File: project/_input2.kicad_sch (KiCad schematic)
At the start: 39 parts, among them J9 input_1x5, Q10 MMBTA44, Q11 MMBTA44, Q12 MMBTA44, Q13 MMBTA44, Q14 MMBTA44, Q15 MMBTA44, Q16 MMBTA44, Q9 MMBTA44, U10 LTV-244-GB-G

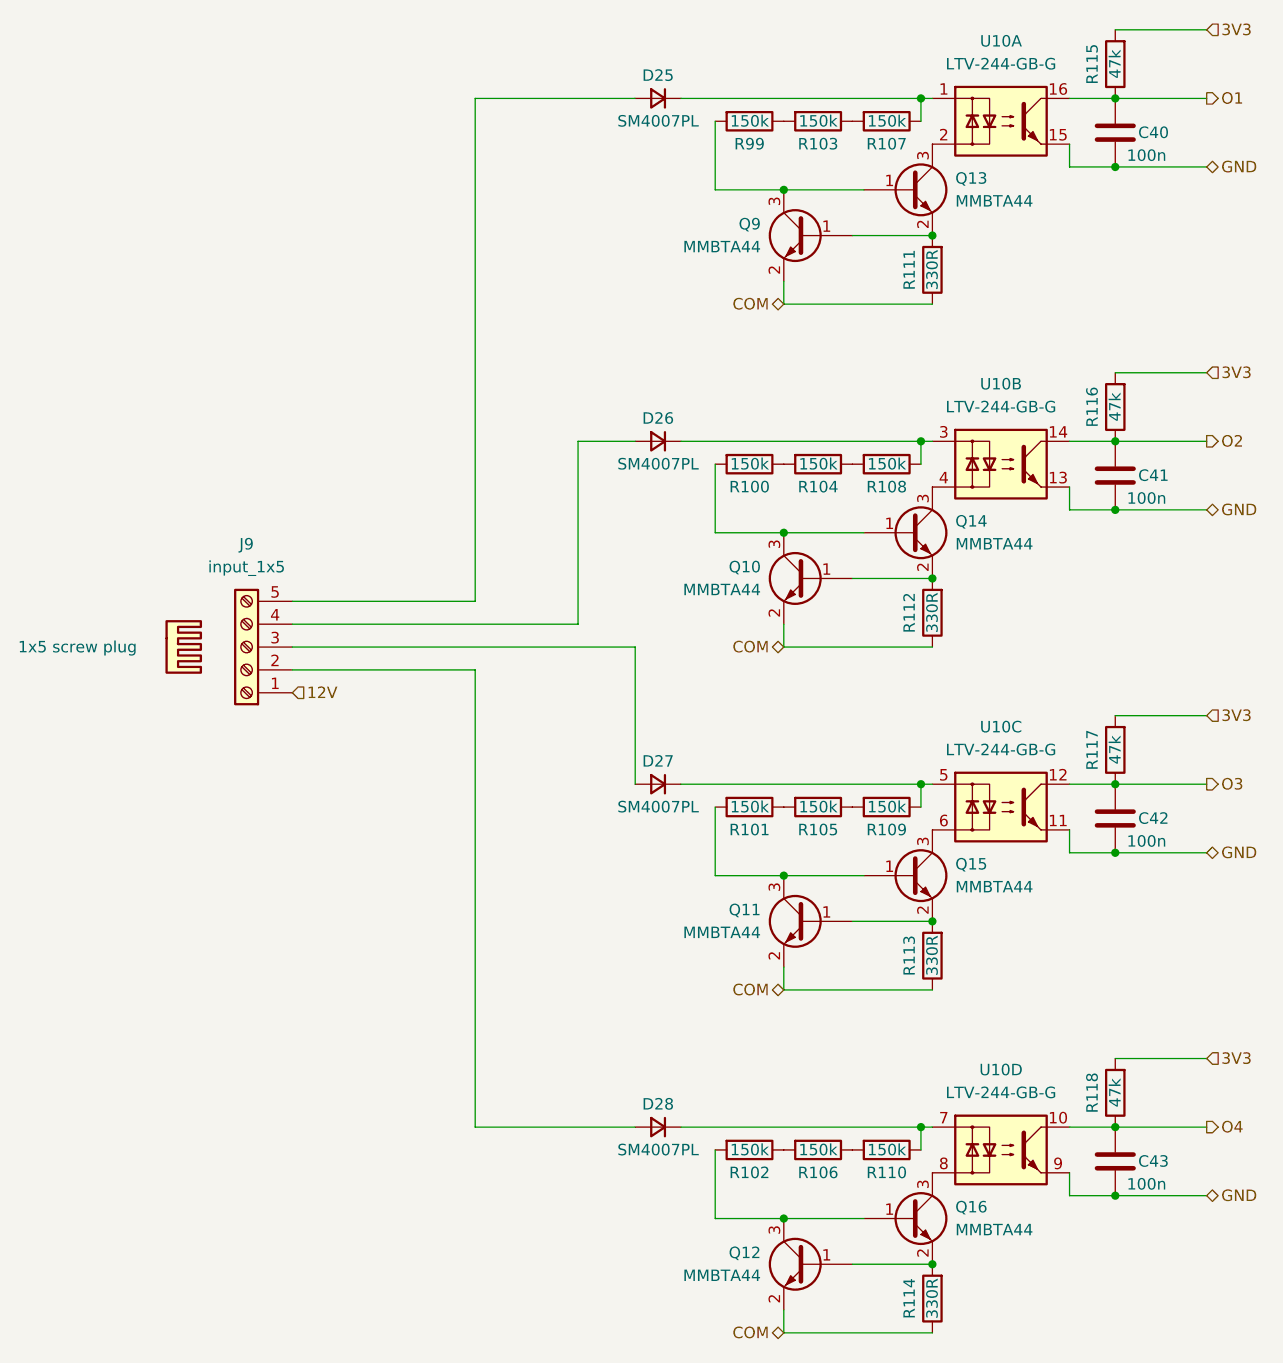
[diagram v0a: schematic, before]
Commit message: refactoring everything to use selected input type
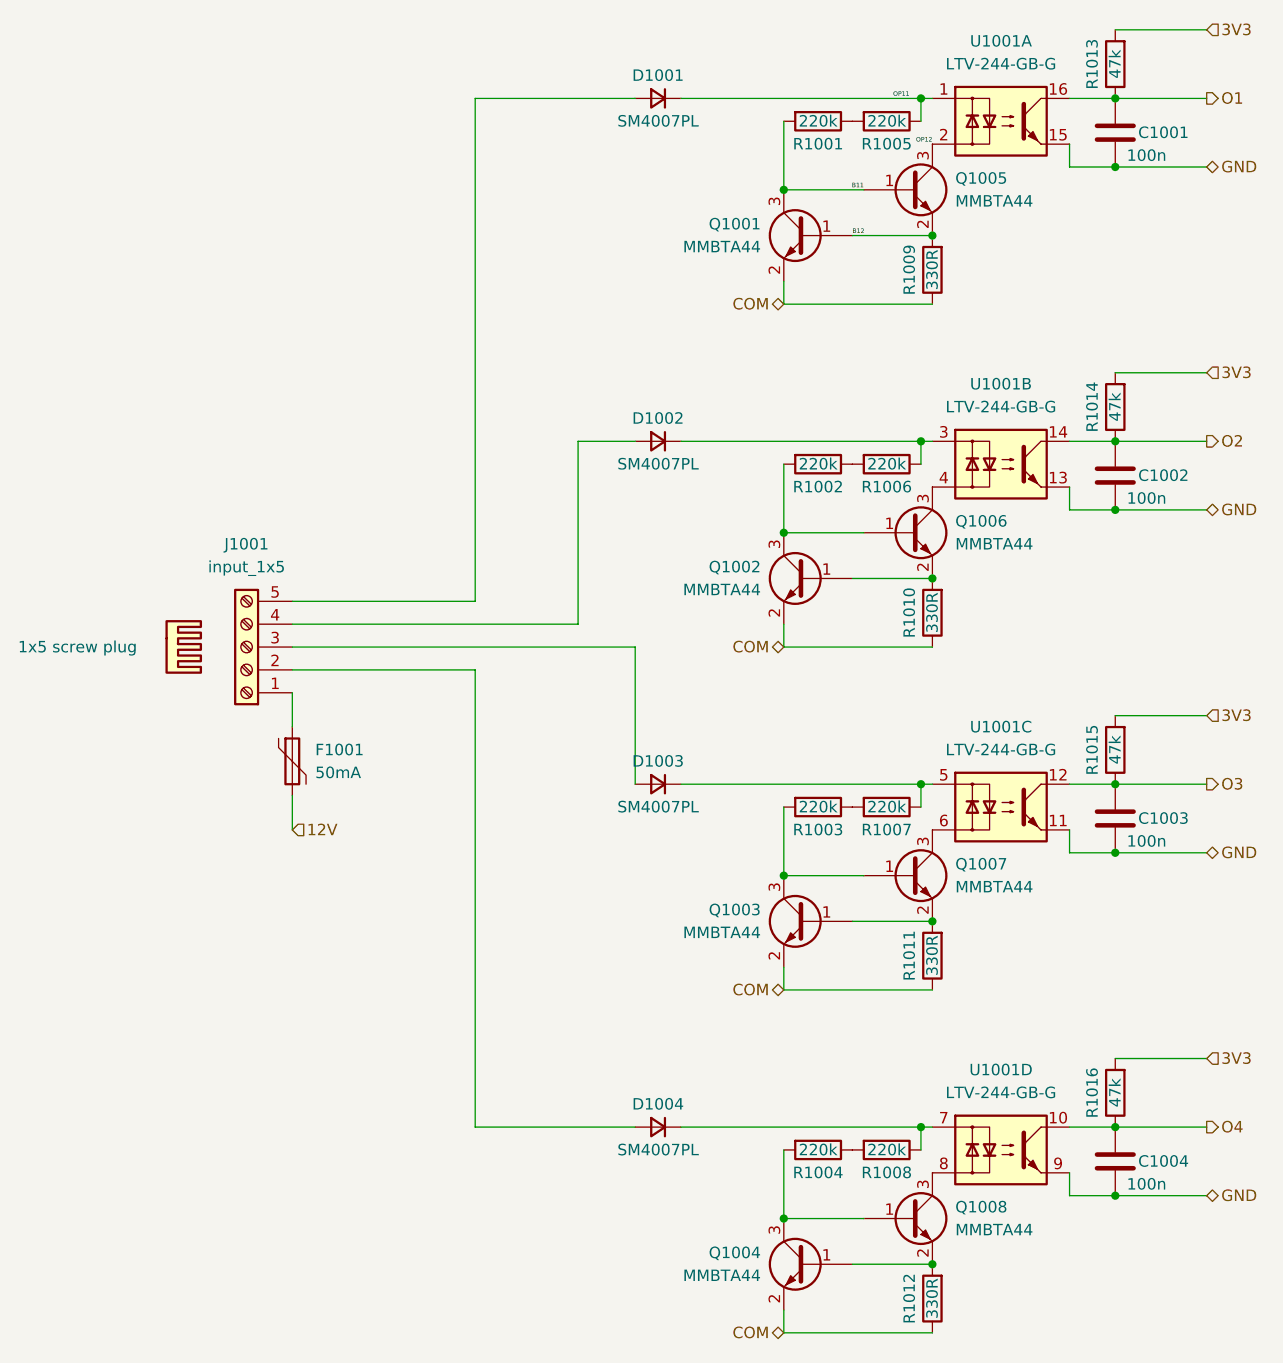
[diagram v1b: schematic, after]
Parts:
- removed C41, C42, C43: 100n, Capacitor_SMD:C_0805_2012Metric_Pad1.18x1.45mm_HandSolder, symbol Device:C
- removed D26, D27, D28: SM4007PL, Diode_SMD:D_SOD-123F, symbol Device:D_Small
- removed Q10, Q11, Q12, Q14, Q15, Q16: MMBTA44, Package_TO_SOT_SMD:SOT-23W, symbol Device:Q_NPN_BEC
- removed R100, R101, R102, R104, R105, R106, R108, R109, R110, R99: 150k, Resistor_SMD:R_0805_2012Metric_Pad1.20x1.40mm_HandSolder, symbol Device:R
- removed R112, R113, R114: 330R, Resistor_SMD:R_0805_2012Metric_Pad1.20x1.40mm_HandSolder, symbol Device:R
- removed R116, R117, R118: 47k, Resistor_SMD:R_0805_2012Metric_Pad1.20x1.40mm_HandSolder, symbol Device:R
- added C1002, C1003, C1004: 100n, Capacitor_SMD:C_0402_1005Metric_Pad0.74x0.62mm_HandSolder, symbol Device:C
- added D1002, D1003, D1004: SM4007PL, Diode_SMD:D_SOD-123F, symbol Device:D_Small
- added F1001: 50mA, Fuse:Fuse_1206_3216Metric_Pad1.42x1.75mm_HandSolder, symbol Device:Polyfuse
- added Q1002, Q1003, Q1004, Q1006, Q1007, Q1008: MMBTA44, Package_TO_SOT_SMD:SOT-23W, symbol Device:Q_NPN_BEC
- added R1002, R1003, R1004, R1006, R1007, R1008: 220k, Resistor_SMD:R_0805_2012Metric_Pad1.20x1.40mm_HandSolder, symbol Device:R
- added R1010, R1011, R1012: 330R, Resistor_SMD:R_0402_1005Metric_Pad0.72x0.64mm_HandSolder, symbol Device:R
- added R1014, R1015, R1016: 47k, Resistor_SMD:R_0402_1005Metric_Pad0.72x0.64mm_HandSolder, symbol Device:R
- C1001: renamed from C40; footprint Capacitor_SMD:C_0805_2012Metric_Pad1.18x1.45mm_HandSolder -> Capacitor_SMD:C_0402_1005Metric_Pad0.74x0.62mm_HandSolder; lcsc# C28233 -> C307331
- R1001: renamed from R103; value 150k -> 220k; lcsc# (none) -> C17556
- R1005: renamed from R107; value 150k -> 220k; lcsc# (none) -> C17556
- R1009: renamed from R111; footprint Resistor_SMD:R_0805_2012Metric_Pad1.20x1.40mm_HandSolder -> Resistor_SMD:R_0402_1005Metric_Pad0.72x0.64mm_HandSolder; lcsc# (none) -> C25104
- R1013: renamed from R115; footprint Resistor_SMD:R_0805_2012Metric_Pad1.20x1.40mm_HandSolder -> Resistor_SMD:R_0402_1005Metric_Pad0.72x0.64mm_HandSolder; lcsc# (none) -> C25792
- renumbered BOM9 to BOM1001, D25 to D1001, J9 to J1001, Q9 to Q1001, Q13 to Q1005, U10 to U1001
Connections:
- net 12V: now also F1001.2; no longer J1001.1 (Pin_1)
- net 3V3: now also R1014.2, R1015.2, R1016.2
- net COM: now also Q1002.2 (E), Q1003.2 (E), Q1004.2 (E), R1010.1, R1011.1, R1012.1
- net GND: now also C1002.2, C1003.2, C1004.2
- net O2: now also C1002.1, R1014.1
- net O3: now also C1003.1, R1015.1
- net O4: now also C1004.1, R1016.1
- net at U1001.3: now also D1002.1 (K), R1006.1
- net at U1001.5: now also D1003.1 (K), R1007.1
- net at U1001.6: now also Q1007.3 (C)
- net B11: now reaches R1001.2
- net B11: now also Q1001.3 (C), Q1005.1 (B)
- net OP11: now reaches D1001.1 (K), R1005.1, U1001.1
- net at J1001.4 (Pin_4): now also D1002.2 (A)
- net OP12: now reaches Q1005.3 (C), U1001.2
- net at U1001.4: now also Q1006.3 (C)
- net at J1001.3 (Pin_3): now also D1003.2 (A)
- net at J1001.2 (Pin_2): now also D1004.2 (A)
- net B12: now reaches Q1001.1 (B), Q1005.2 (E), R1009.2
- net at U1001.8: now also Q1008.3 (C)
- net at U1001.7: now also D1004.1 (K), R1008.1
- new net: Q1003.3 (C), Q1007.1 (B), R1003.2
- new net: Q1003.1 (B), Q1007.2 (E), R1011.2
- new net: Q1004.1 (B), Q1008.2 (E), R1012.2
- new net: Q1004.3 (C), Q1008.1 (B), R1004.2
- new net: Q1002.3 (C), Q1006.1 (B), R1002.2
- new net: Q1002.1 (B), Q1006.2 (E), R1010.2
- new net: R1003.1, R1007.2
- new net: F1001.1, J1001.1 (Pin_1)
- new net: R1004.1, R1008.2
- new net: R1002.1, R1006.2

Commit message: replacing thermometer
* Switching to TMP102 as TMP101 is no longer available
* bumping up version
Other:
- company: (none) -> makerspace.lt
- title: (none) -> WormControl-Input32-InputBoard
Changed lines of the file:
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@@
 (kicad_sch (version 20211123) (generator eeschema)
   (paper "A4")
+  (title_block
+    (title "WormControl-Input32-InputBoard")
+    (date "2026-03-19")
+    (rev "0.3")
+    (company "makerspace.lt")
+  )
   (junction (at 154.94 45.72) (diameter 0) (color 0 0 0 0)
   )

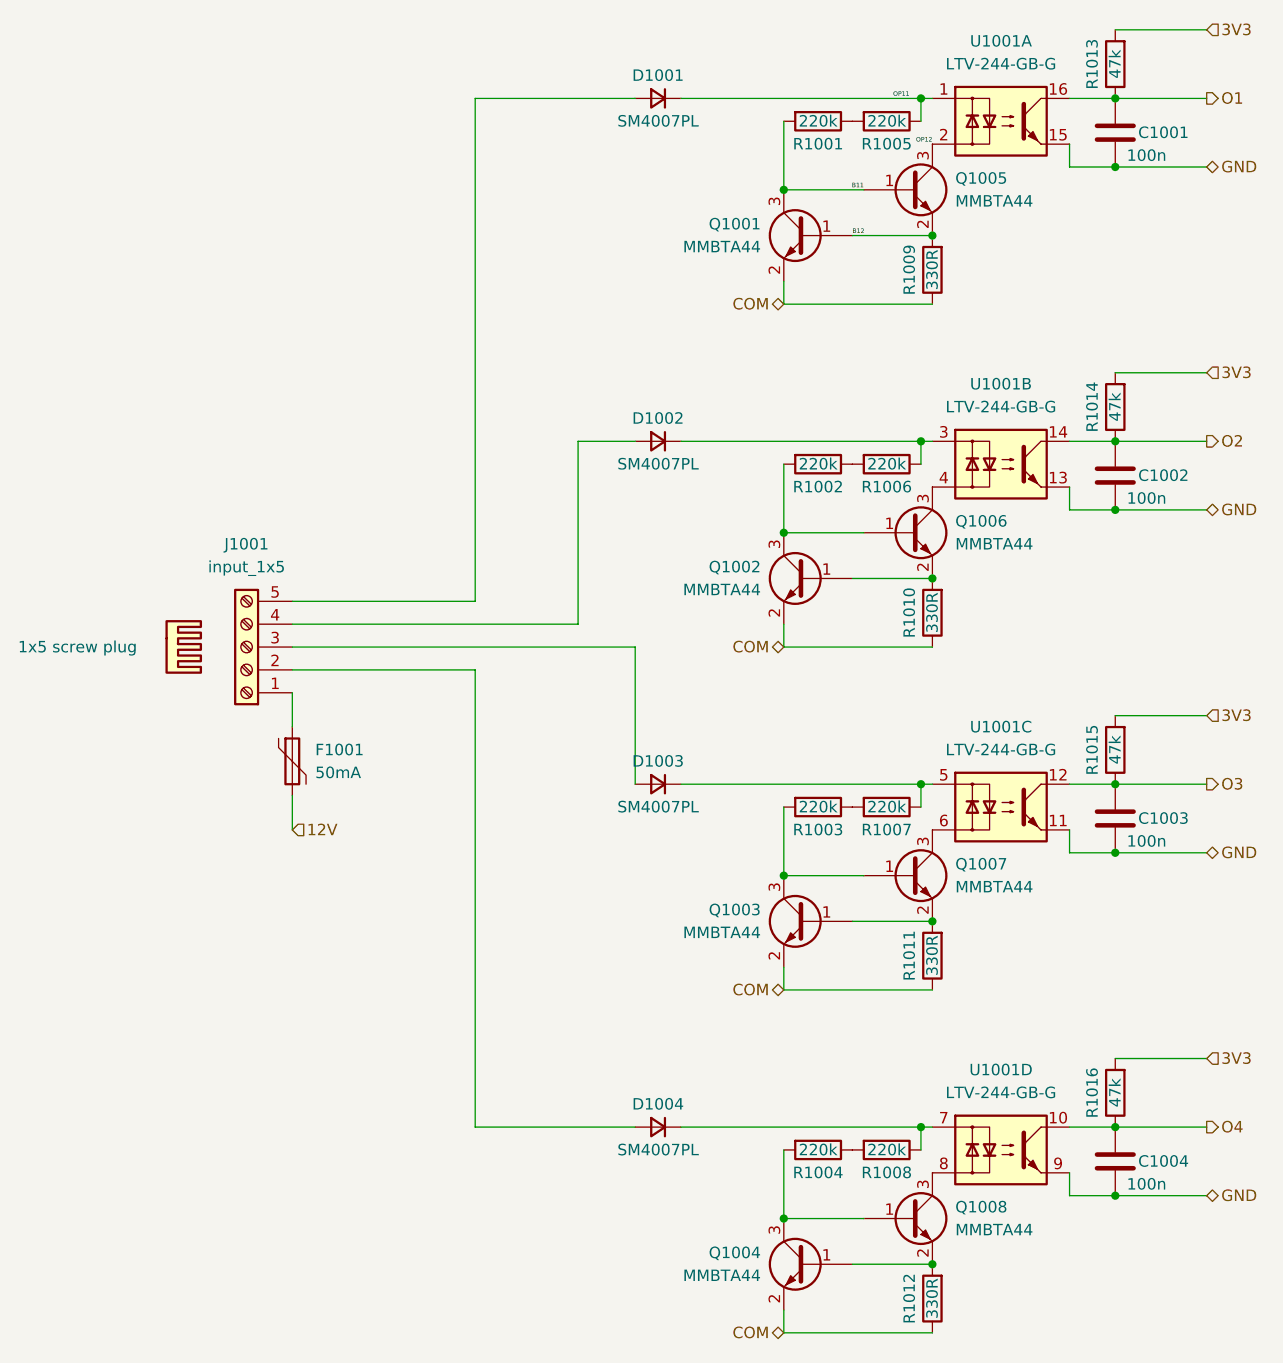
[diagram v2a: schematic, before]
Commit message: fixing tmp102 pinout
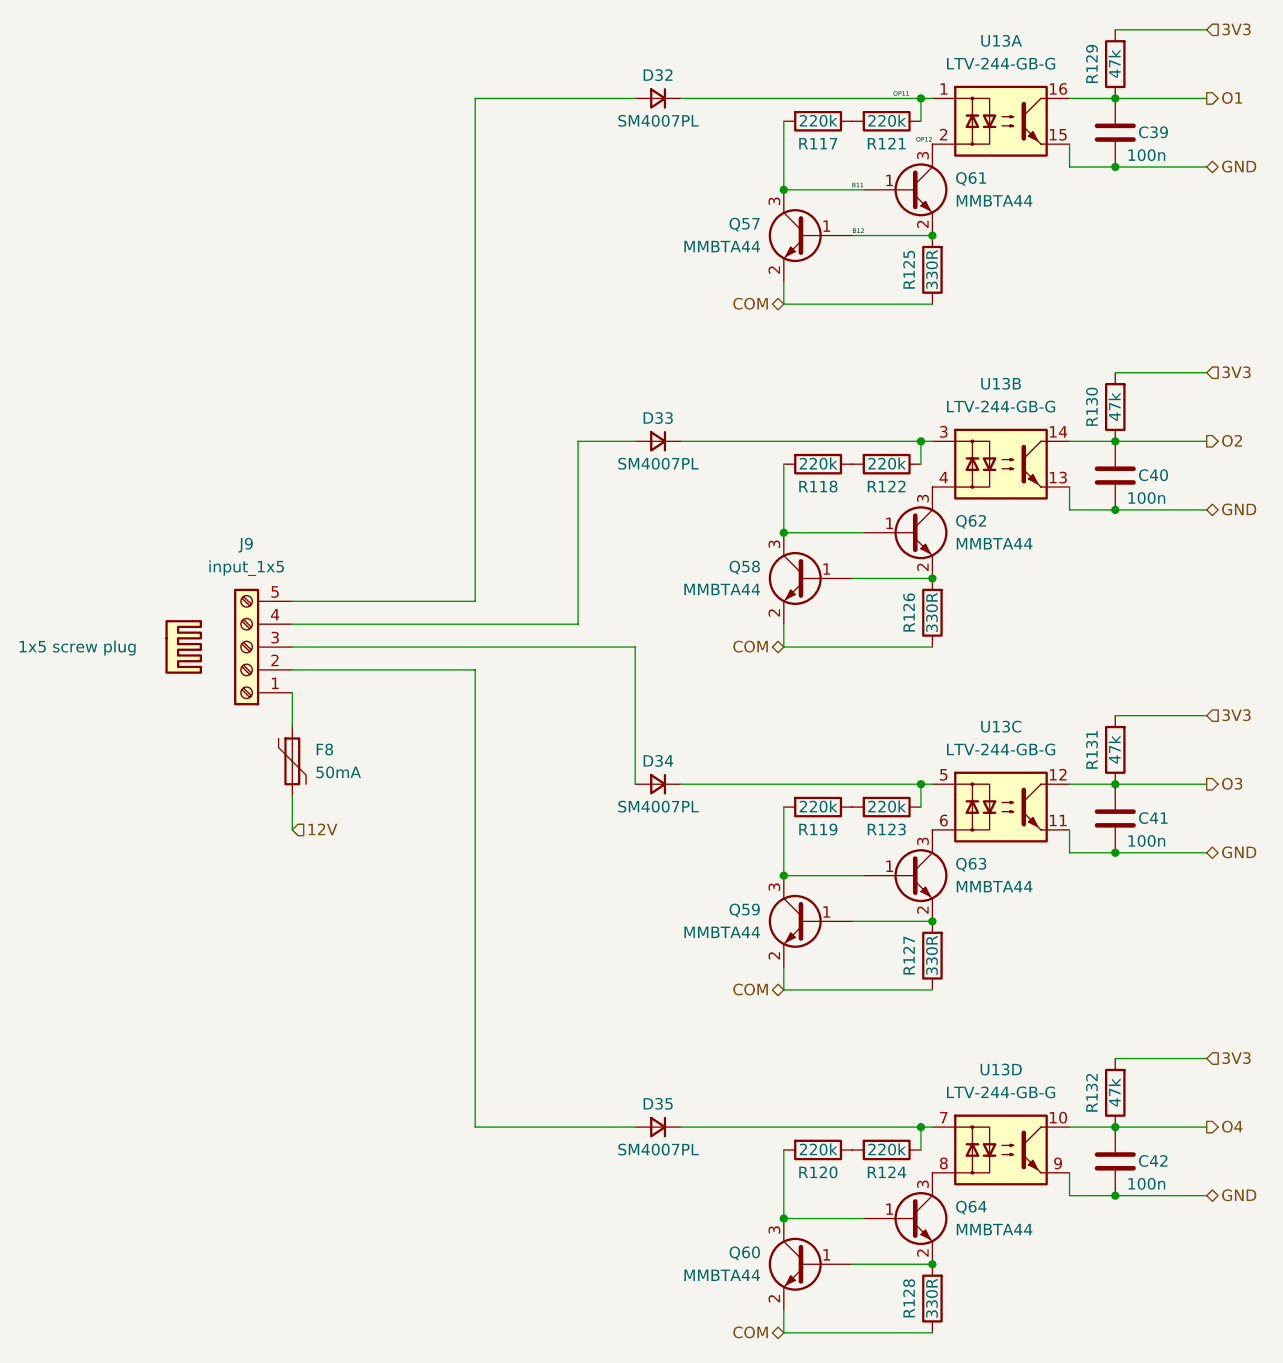
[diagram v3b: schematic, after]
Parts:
- renumbered BOM1001 to BOM9, C1001 to C39, C1002 to C40, C1003 to C41, C1004 to C42, D1001 to D32, D1002 to D33, D1003 to D34, D1004 to D35, F1001 to F8, J1001 to J9, Q1001 to Q57, Q1002 to Q58, Q1003 to Q59, Q1004 to Q60, Q1005 to Q61, Q1006 to Q62, Q1007 to Q63, Q1008 to Q64, R1001 to R117, R1002 to R118, R1003 to R119, R1004 to R120, R1005 to R121, R1006 to R122, R1007 to R123, R1008 to R124, R1009 to R125, R1010 to R126, R1011 to R127, R1012 to R128, R1013 to R129, R1014 to R130, R1015 to R131, R1016 to R132, U1001 to U13
